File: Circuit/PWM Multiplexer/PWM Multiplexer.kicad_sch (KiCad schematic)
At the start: 63 parts, among them Q1 S8050, Q10 S8050, Q11 S8050, Q12 S8050, Q13 S8050, Q14 S8050, Q2 S8050, Q3 S8050, Q4 S8050, Q5 S8050, Q6 S8050, Q7 S8050, Q8 S8050, Q9 S8050, U1 74HC137, U2 74HC137, U3 L7805

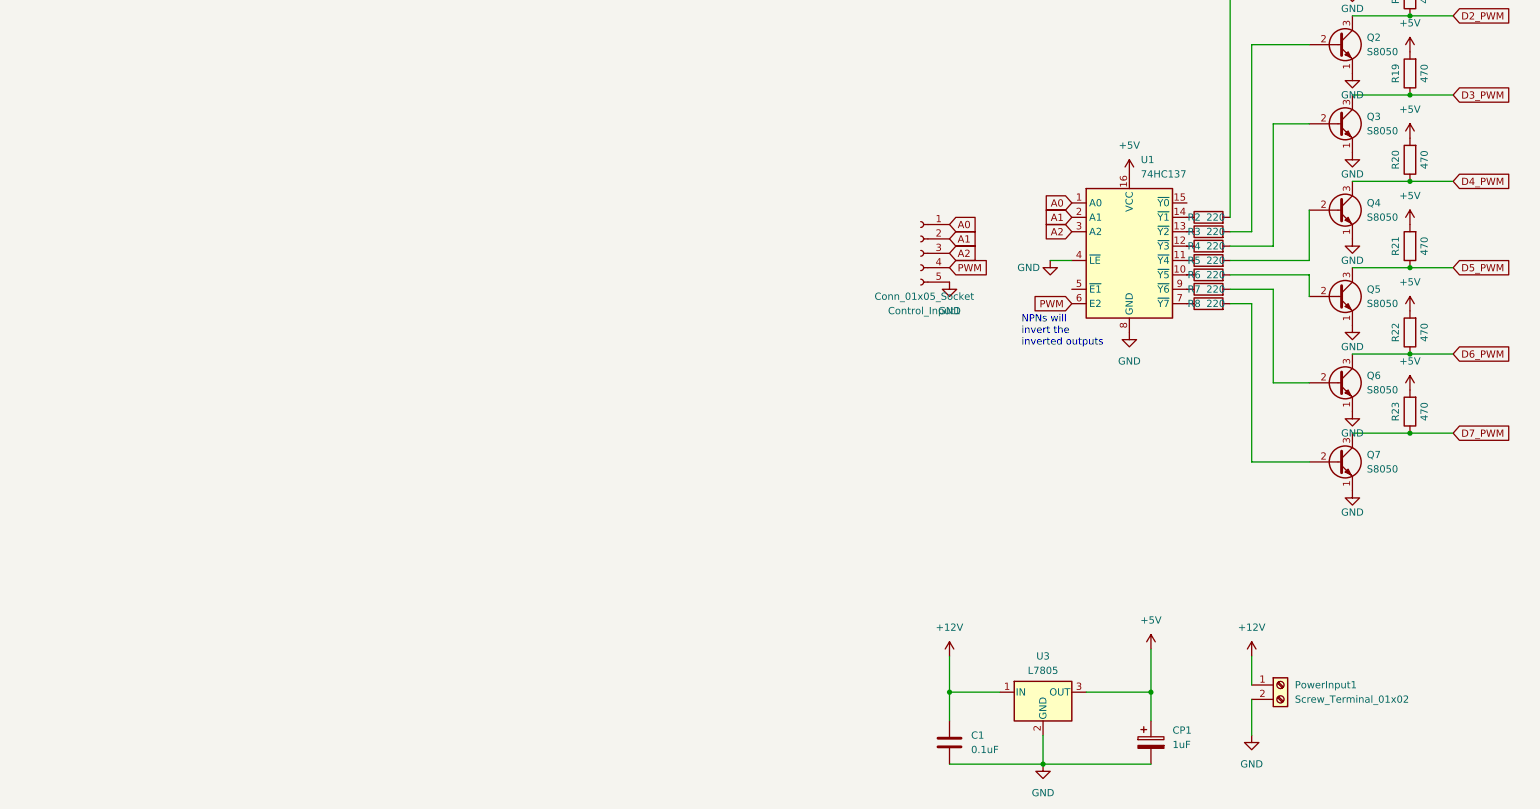
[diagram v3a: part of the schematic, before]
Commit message: Implemented Isolators in PWM Mutliplexer
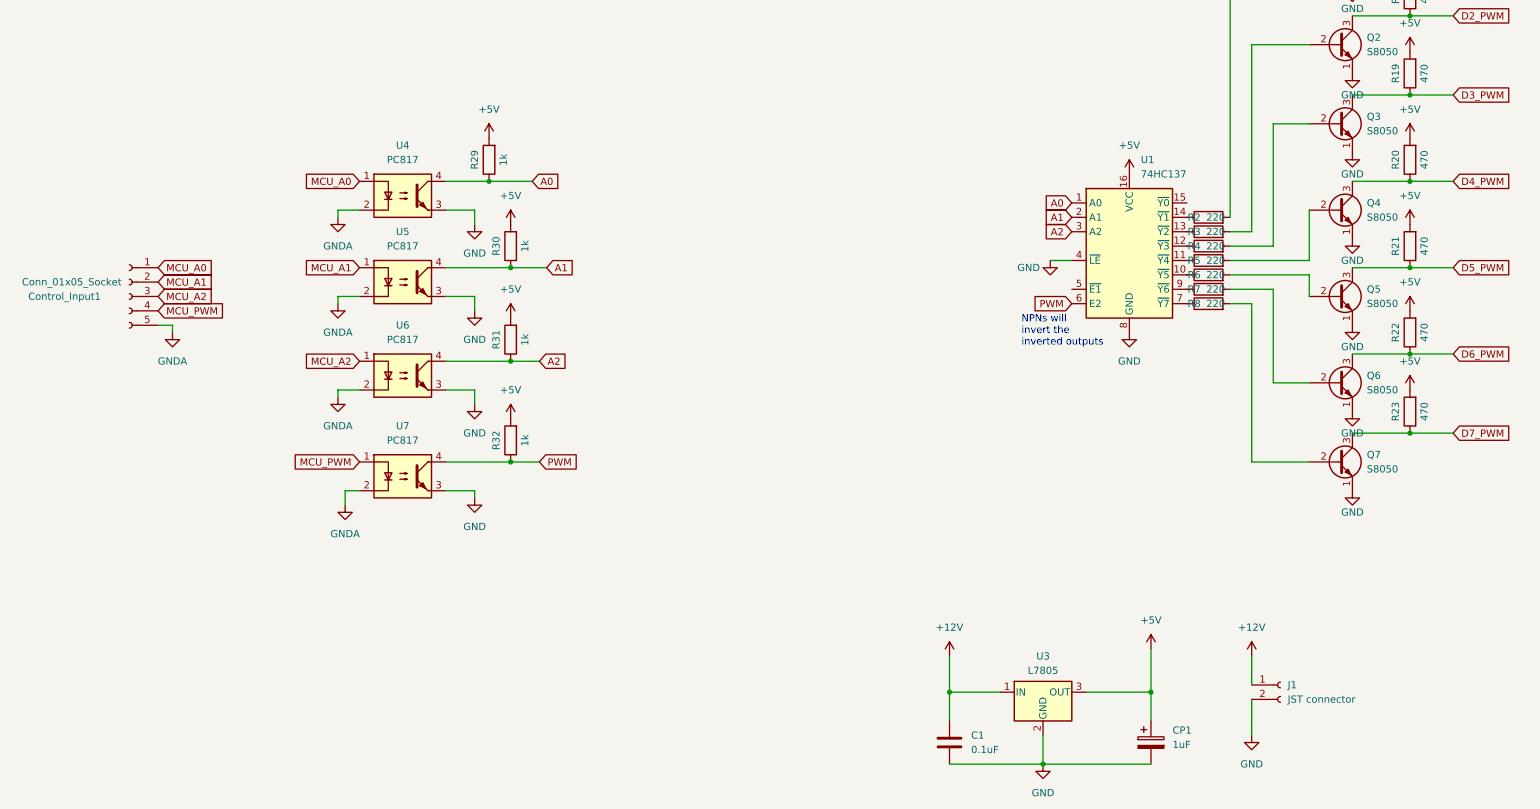
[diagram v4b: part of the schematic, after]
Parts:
- removed PowerInput1: Screw_Terminal_01x02, TerminalBlock:TerminalBlock_bornier-2_P5.08mm, symbol Connector:Screw_Terminal_01x02
- added J1: JST connector, Connector_PinSocket_2.54mm:PinSocket_1x02_P2.54mm_Horizontal, symbol Connector:Conn_01x02_Socket
- added R29, R30, R31, R32: 1k, Resistor_THT:R_Axial_DIN0207_L6.3mm_D2.5mm_P10.16mm_Horizontal, symbol Device:R
- added U4, U5, U6, U7: PC817, Package_DIP:DIP-4_W7.62mm, symbol Isolator:PC817
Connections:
- net +12V: now also J1.1 (Pin_1)
- net +5V: now also R29.2, R30.2, R31.2, R32.2
- net A0: now also R29.1, U4.4; no longer Control_Input1.1 (Pin_1)
- net A1: now also R30.1, U5.4; no longer Control_Input1.2 (Pin_2)
- net A2: now also R31.1, U6.4; no longer Control_Input1.3 (Pin_3)
- net GND: now also J1.2 (Pin_2), U4.3, U5.3, U6.3, U7.3; no longer Control_Input1.5 (Pin_5)
- net PWM: now also R32.1, U7.4; no longer Control_Input1.4 (Pin_4)
- new net GNDA: Control_Input1.5 (Pin_5), U4.2, U5.2, U6.2, U7.2
- new net MCU_A0: Control_Input1.1 (Pin_1), U4.1
- new net MCU_A1: Control_Input1.2 (Pin_2), U5.1
- new net MCU_A2: Control_Input1.3 (Pin_3), U6.1
- new net MCU_PWM: Control_Input1.4 (Pin_4), U7.1
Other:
- moved on the sheet: Control_Input1

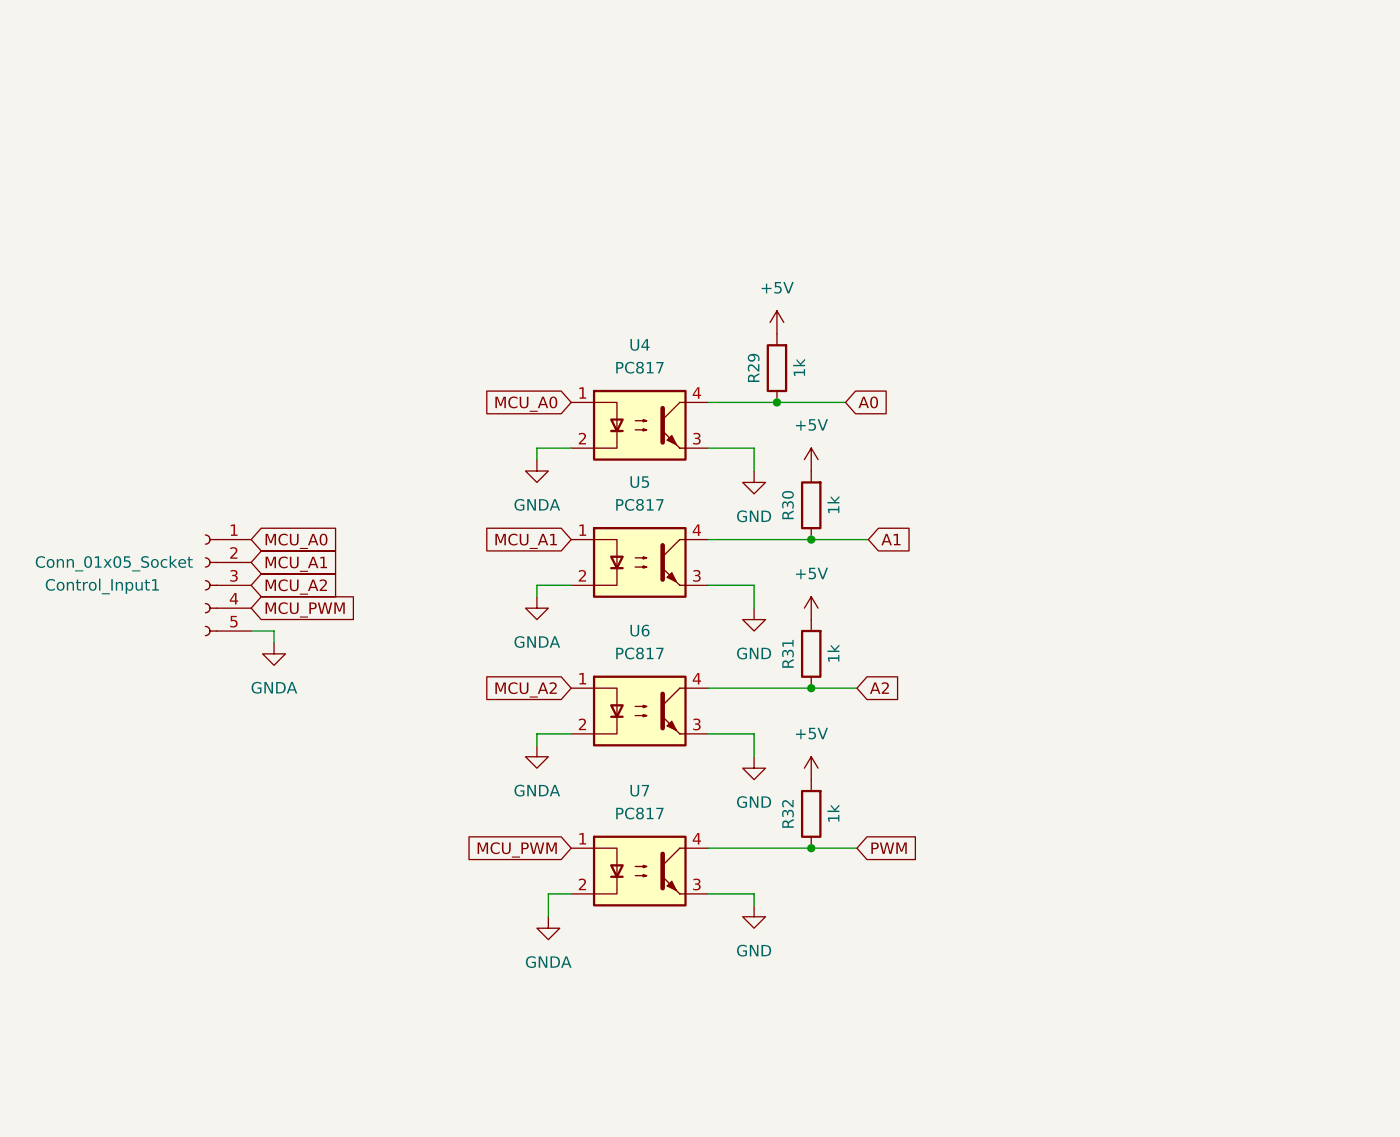
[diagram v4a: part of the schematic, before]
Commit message: added optical isolation to PWM demultiplexer circuit schematic
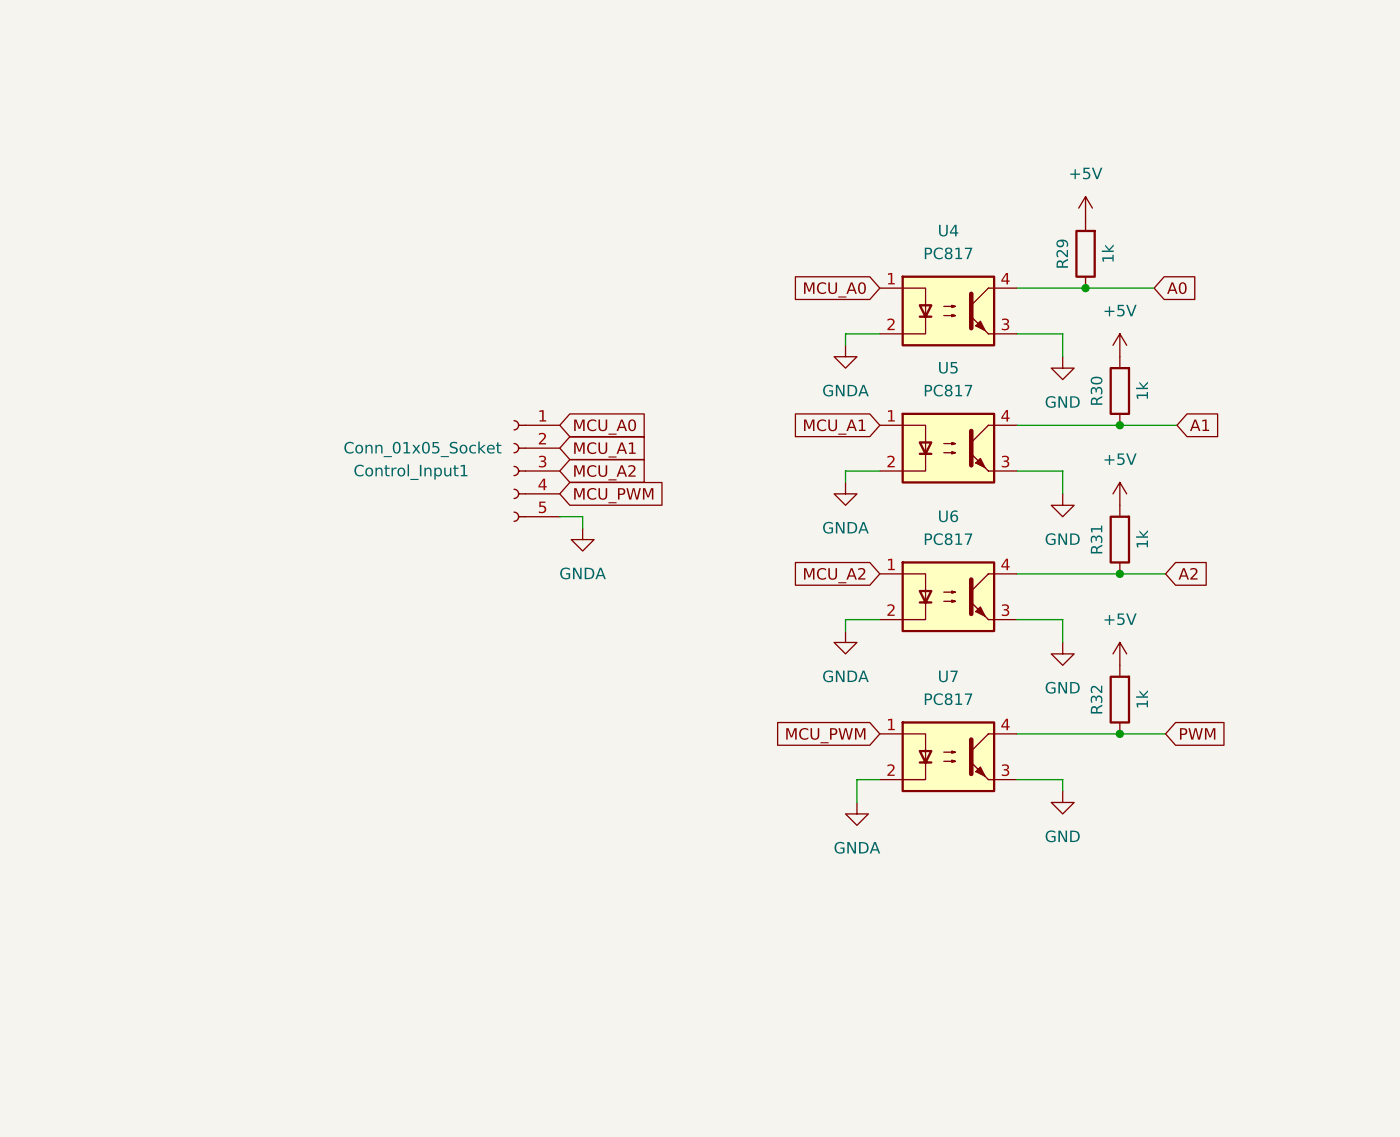
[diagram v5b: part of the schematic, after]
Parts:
- J1: footprint Connector_PinSocket_2.54mm:PinSocket_1x02_P2.54mm_Horizontal -> Connector_JST:JST_EH_S2B-EH_1x02_P2.50mm_Horizontal
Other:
- moved on the sheet: Control_Input1, R29, R30, R31, R32, U4, U5, U6, U7
